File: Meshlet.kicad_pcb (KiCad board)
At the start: 2 copper layers, 60.2 x 39 mm, 98 parts, among them J1 Ext. Notif. Header, J10 STEMMA QT I2C, J11 GPIO Exp., J12 I2C PINHEADER, J2 USB_C_Receptacle_USB2.0_16P, J3 Ext. Power Header, J4 Batt. Header (JST-PH 2.0), J5 SWD, J6 Batt. Header (Picoblade 1.25), J7 GPS Header, J8 User Btn Header, J9 Power Switch, Q1 AO3400A, SW1 BOOTSEL, SW3 RST, U1 W25Q32JVZP, U2 XC6206PxxxMR, U3 RP2350_60QFN, U4 INA3221, U5 BME280, U6 Wio-SX1262, U7 USBLC6-2SC6, U8 BQ24074RGT, Y1 12.000MHz

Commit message: appease the trademark gods
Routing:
- net Net-(J9-Pin_1): track 14.3 -> 14.9 mm
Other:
- board text added: "HEY!"
- board text added: "PUT ME BACK!"

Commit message: docs
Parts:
- J7: footprint Connector_PinHeader_1.27mm:PinHeader_1x04_P1.27mm_Vertical -> Connector_PinHeader_1.27mm:PinHeader_1x05_P1.27mm_Vertical
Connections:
- U3 pad 8: unconnected-(U3-GPIO5-Pad8) -> GPS_EN
- U4 pad 5: GND -> I2C_SDA
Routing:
- net GPS_EN: track 0.00 -> 21.0 mm, vias 0 -> 1
- net I2C_SDA: track 107.4 -> 112.0 mm, vias 3 -> 4
- net Net-(U3-RUN): track 41.7 -> 44.7 mm
- net GND: track 23.7 -> 21.1 mm
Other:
- board text added: "3V"
- board text added: ":"
- board text added: "EN"
- board text added: "I HOPE YOU HAVE A LONG ENOUGH USB CABLE"
- board text added: "USR BTN"
- board text added: "https://5panel.dance/meshlet"
- board text added: "×1"

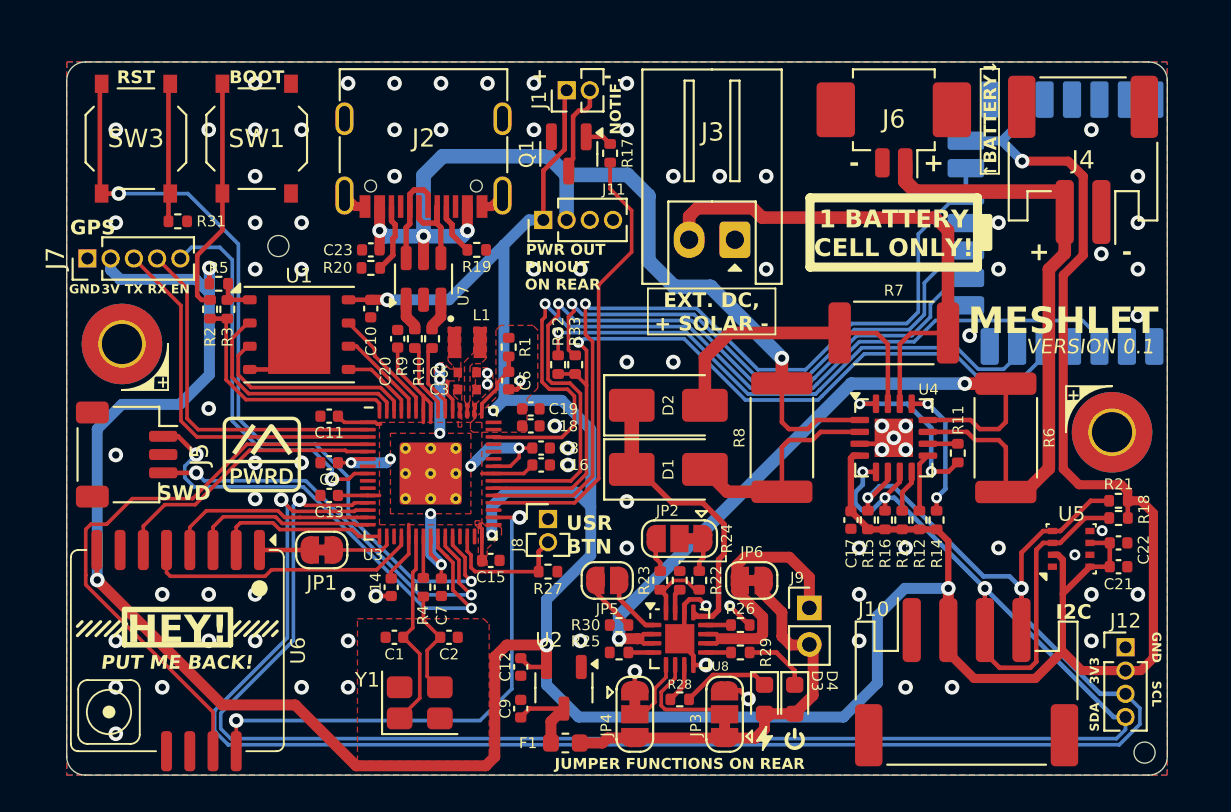
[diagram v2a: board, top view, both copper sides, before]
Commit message: Fixed stemma port pin order, more touchups
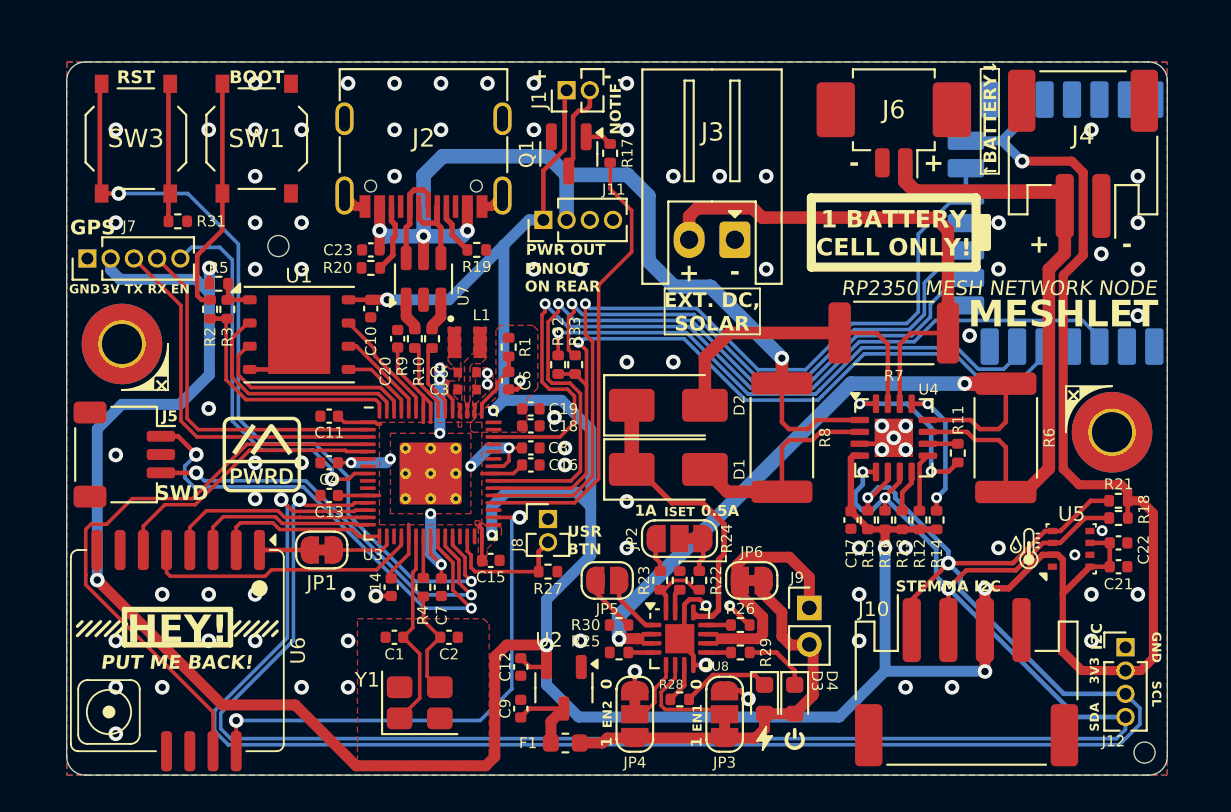
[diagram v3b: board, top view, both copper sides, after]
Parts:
- removed ?: , 
- added REF**: ToolingHole_1.152mm, MountingHole:ToolingHole_1.152mm, F.Cu at (121.8, 64.2)
- moved C16 0.57 mm to (135.6, 76.2)
- moved C8 0.56 mm to (135.6, 75.3)
- moved J4 0.33 mm to (165.8, 59.2)
- moved J5 0.13 mm to (113.4, 75.6)
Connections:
- J10 pad 1: GND -> I2C_SCL
- J10 pad 2: +3V3 -> I2C_SDA
- J10 pad 3: I2C_SDA -> +3V3
- J10 pad 4: I2C_SCL -> GND
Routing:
- net I2C_SCL: track 105.6 -> 110.2 mm
- net I2C_SDA: track 112.0 -> 109.1 mm
- net +3V3: track 256.3 -> 257.4 mm, vias 8 -> 10
- net +1V1: track 21.3 -> 20.3 mm
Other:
- board text added: "0"
- board text added: "0.5A"
- board text added: "1"
- board text added: "1A"
- board text added: "EN1"
- board text added: "EN2"
- board text added: "EXT. DC, SOLAR"
- board text added: "ISET"
- board text added: "RP2350 MESH NETWORK NODE"
- board text added: "STEMMA I2C"
- board text added: "V0.1"
- board text added: "https://5panel.dance/Meshlet"
- board text added: "×"
- board text removed: "EXT. DC, + SOLAR -"
- board text removed: "JUMPER FUNCTIONS ON REAR"
- board text removed: "https://5panel.dance/meshlet"

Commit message: Ground fill thermal spoke bug workaround for RM2
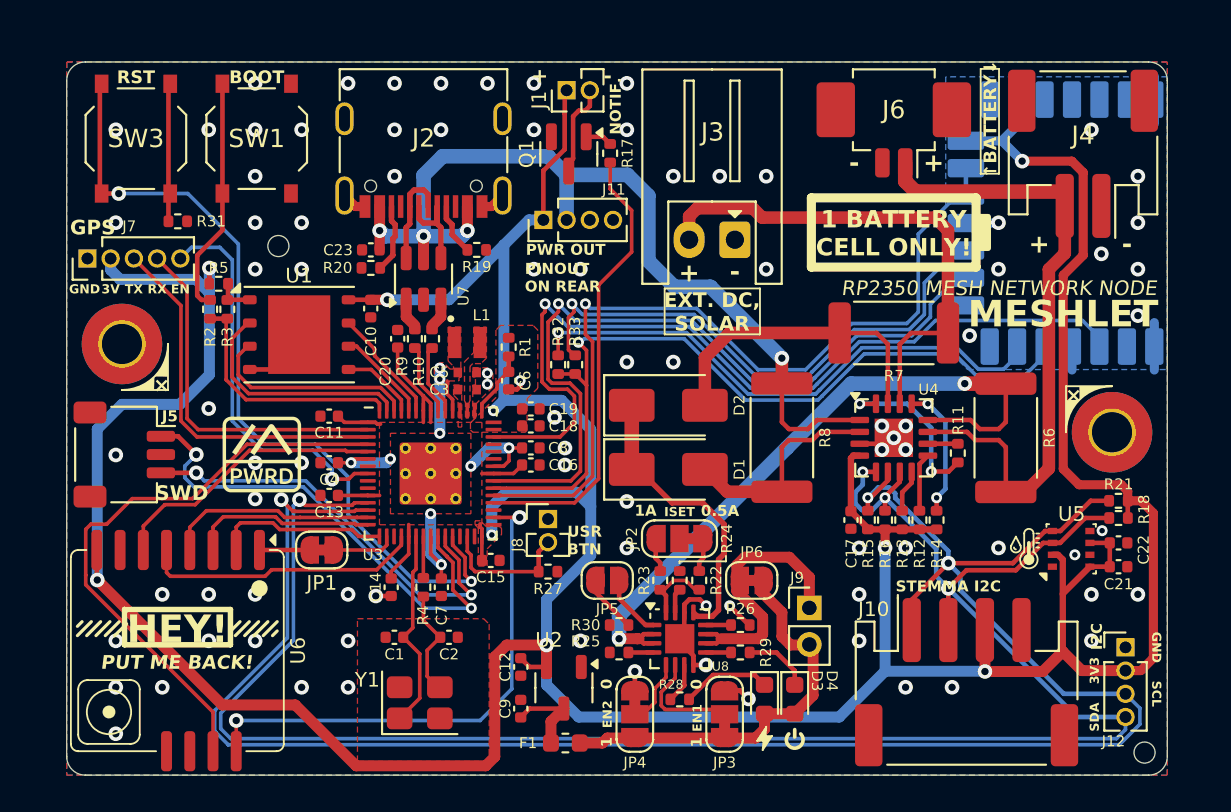
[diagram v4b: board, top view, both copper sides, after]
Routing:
- net GND: track 21.1 -> 29.6 mm
- net +3V3: track 257.4 -> 255.4 mm, vias 10 -> 9
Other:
- board text added: "GP0"
- board text added: "GP1"
- board text added: "GP22"
- board text added: "GP5"
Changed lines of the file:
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@@
 			(at -1.375 -1.375)
 			(size 0.6 0.6)
-			(drill 0.25)
+			(drill 0.3)
 			(layers "*.Cu")
 			(remove_unused_layers no)
@@
 			(at -1.375 0)
 			(size 0.6 0.6)
-			(drill 0.25)
+			(drill 0.3)
 			(layers "*.Cu")
 			(remove_unused_layers no)
@@
 			(at -1.375 1.375)
 			(size 0.6 0.6)
-			(drill 0.25)
+			(drill 0.3)
 			(layers "*.Cu")
 			(remove_unused_layers no)
@@
 			(at 0 -1.375)
 			(size 0.6 0.6)
-			(drill 0.25)
+			(drill 0.3)
 			(layers "*.Cu")
 			(remove_unused_layers no)
@@
 			(at 0 0)
 			(size 0.6 0.6)
-			(drill 0.25)
+			(drill 0.3)
 			(layers "*.Cu")
 			(remove_unused_layers no)
@@
 			(at 0 1.375)
 			(size 0.6 0.6)
-			(drill 0.25)
+			(drill 0.3)
 			(layers "*.Cu")
 			(remove_unused_layers no)
@@
 			(at 1.375 -1.375)
 			(size 0.6 0.6)
-			(drill 0.25)
+			(drill 0.3)
 			(layers "*.Cu")
 			(remove_unused_layers no)
@@
 			(at 1.375 0)
 			(size 0.6 0.6)
-			(drill 0.25)
+			(drill 0.3)
 			(layers "*.Cu")
 			(remove_unused_layers no)
@@
 			(at 1.375 1.375)
 			(size 0.6 0.6)
-			(drill 0.25)
+			(drill 0.3)
 			(layers "*.Cu")
 			(remove_unused_layers no)
@@
 			(pinfunction "1")
 			(pintype "passive")
+			(clearance 0.2)
 		)
 		(pad "2" smd roundrect
@@
 			(pinfunction "3")
 			(pintype "passive")
+			(clearance 0.2)
 		)
 		(pad "4" smd roundrect
@@
 			(net 1 "XIN")
 			(pintype "passive")
+			(clearance 0.2)
 		)
 		(embedded_fonts no)
@@
 			(net 3 "Net-(C2-Pad2)")
 			(pintype "passive")
+			(clearance 0.2)
 		)
 		(embedded_fonts no)
@@
 		)
 	)
+	(gr_text "GP22"
+		(at 139.827 56.7563 270)
+		(layer "B.SilkS")
+		(effects
+			(font
+				(size 0.5 0.5)
+				(thickness 0.125)
+				(bold yes)
+			)
+			(justify left bottom mirror)
+		)
+	)
 	(gr_text "RP2350 MESH NETWORK NODE RP2350 MESH NETWORK NODE RP2350 MESH"
 		(at 155.35 78.025 45)
@@
 		)
 	)
+	(gr_text "GP0"
+		(at 115.2144 65.6336 90)
+		(layer "B.SilkS")
+		(effects
+			(font
+				(size 0.5 0.5)
+				(thickness 0.125)
+				(bold yes)
+			)
+			(justify left mirror)
+		)
+	)
 	(gr_text "GND"
 		(at 138.86 60.53 90)
@@
 		)
 	)
+	(gr_text "GP1"
+		(at 113.9444 65.6336 90)
+		(layer "B.SilkS")
+		(effects
+			(font
+				(size 0.5 0.5)
+				(thickness 0.125)
+				(bold yes)
+			)
+			(justify left mirror)
+		)
+	)
+	(gr_text "GP5"
+		(at 116.4844 65.6336 90)
+		(layer "B.SilkS")
+		(effects
+			(font
+				(size 0.5 0.5)
+				(thickness 0.125)
+				(bold yes)
+			)
+			(justify left mirror)
+		)
+	)
 	(gr_text "×1"
 		(at 134.2771 65.8622 0)
@@
 	)
 	(segment
+		(start 159.4228 62.9856)
+		(end 161.185518 62.9856)
+		(width 0.5)
+		(layer "B.Cu")
+		(net 2)
+	)
+	(segment
+		(start 169.7228 56.2356)
+		(end 169.7228 56.0578)
+		(width 0.5)
+		(layer "B.Cu")
+		(net 2)
+	)
+	(segment
+		(start 169.7228 56.2356)
+		(end 169.7228 54.9656)
+		(width 0.5)
+		(layer "B.Cu")
+		(net 2)
+	)
+	(segment
+		(start 165.2228 69.7356)
+		(end 165.2228 71.0184)
+		(width 0.5)
+		(layer "B.Cu")
+		(net 2)
+	)
+	(segment
+		(start 169.7228 69.7356)
+		(end 169.7228 71.0184)
+		(width 0.5)
+		(layer "B.Cu")
+		(net 2)
+	)
+	(segment
+		(start 161.185518 62.9856)
+		(end 161.205518 62.9656)
+		(width 0.5)
+		(layer "B.Cu")
+		(net 2)
+	)
+	(segment
+		(start 169.7228 69.7356)
+		(end 169.7228 68.4276)
+		(width 0.5)
+		(layer "B.Cu")
+		(net 2)
+	)
+	(segment
+		(start 169.7228 56.2356)
+		(end 169.7228 57.5564)
+		(width 0.5)
+		(layer "B.Cu")
+		(net 2)
+	)
+	(segment
 		(start 129.76 83.404657)
 		(end 129.76 84.709508)
@@
 	)
 	(segment
-		(start 164.1512 81.1224)
-		(end 163.609554 81.1224)
-		(width 0.35)
-		(layer "F.Cu")
-		(net 4)
-	)
-	(segment
 		(start 132.86 79.594176)
 		(end 132.86 79.429308)
@@
 	)
 	(segment
+		(start 165.7604 87.4522)
+		(end 164.719 86.4108)
+		(width 0.6)
+		(layer "F.Cu")
+		(net 4)
+	)
+	(segment
 		(start 135.561899 87.2553)
 		(end 135.084399 86.7778)
@@
 	)
 	(segment
-		(start 164.719 86.4108)
-		(end 164.6936 86.4108)
-		(width 0.5)
-		(layer "F.Cu")
-		(net 4)
-	)
-	(segment
 		(start 126.7225 73.879308)
 		(end 127.145132 73.879308)
@@
 	)
 	(segment
+		(start 163.6268 87.503)
+		(end 164.719 86.4108)
+		(width 0.6)
+		(layer "F.Cu")
+		(net 4)
+	)
+	(segment
 		(start 162.4965 59.6011)
 		(end 165.2143 59.6011)
@@
 	)
 	(segment
+		(start 168.148 87.4522)
+		(end 165.7604 87.4522)
+		(width 0.6)
+		(layer "F.Cu")
+		(net 4)
+	)
+	(segment
 		(start 126.7225 77.879308)
 		(end 126.719592 77.8764)
@@
 	)
 	(segment
-		(start 161.775554 82.9564)
-		(end 160.4612 82.9564)
-		(width 0.35)
-		(layer "F.Cu")
-		(net 4)
-	)
-	(segment
 		(start 127.145132 73.879308)
 		(end 127.245132 73.979308)
@@
 	)
 	(segment
-		(start 163.609554 81.1224)
-		(end 161.775554 82.9564)
-		(width 0.35)
-		(layer "F.Cu")
-		(net 4)
-	)
-	(segment
 		(start 111.9124 80.8624)
 		(end 111.91 80.86)
@@
 	)
 	(segment
-		(start 160.4612 85.2372)
-		(end 160.4612 82.9564)
-		(width 0.6)
-		(layer "F.Cu")
-		(net 4)
-	)
-	(segment
-		(start 165.7604 87.4522)
-		(end 168.148 87.4522)
-		(width 0.5)
-		(layer "F.Cu")
-		(net 4)
-	)
-	(segment
 		(start 164.7444 65.8368)
 		(end 164.7444 76.4286)
@@
 	)
 	(segment
-		(start 164.719 86.4108)
-		(end 165.7604 87.4522)
-		(width 0.5)
-		(layer "F.Cu")
-		(net 4)
-	)
-	(segment
 		(start 130.16 73.241808)
 		(end 130.16 73.885308)
@@
 	)
 	(segment
+		(start 160.4645 87.503)
+		(end 163.6268 87.503)
+		(width 0.6)
+		(layer "F.Cu")
+		(net 4)
+	)
+	(segment
 		(start 164.4598 81.1224)
 		(end 164.719 81.3816)
@@
 	)
 	(via
-		(at 160.4612 82.9564)
-		(size 0.8)
-		(drill 0.4)
-		(layers "F.Cu" "B.Cu")
-		(net 4)
-	)
-	(via
 		(at 133.5024 80.0354)
 		(size 0.6)
@@
 	(segment
 		(start 153.1457 71.7643)
+		(end 149.64695 75.26305)
+		(width 0.8)
+		(layer "B.Cu")
+		(net 44)
+	)
+	(segment
+		(start 149.64695 75.26305)
 		(end 140.462 84.448)
 		(width 0.8)
@@
 		(priority 2)
 		(connect_pads
-			(clearance 0.2)
+			(clearance 0.1)
 		)
 		(min_thickness 0.2)
@@
 		(layers "F.Cu" "B.Cu")
 		(hatch edge 0.5)
-		(connect_pads thru_hole_only
+		(connect_pads
 			(clearance 0.1)
 		)
@@
 			)
 		)
+	)
+	(zone
+		(net 2)
+		(net_name "GND")
+		(layer "B.Cu")
+		(hatch edge 0.508)
+		(priority 9)
+		(connect_pads
+			(clearance 0.2)
+		)
+		(min_thickness 0.2)
+		(filled_areas_thickness no)
+		(fill yes
+			(thermal_gap 0.3)
+			(thermal_bridge_width 0.5)
+			(island_removal_mode 1)
+			(island_area_min 10)
+		)
+		(polygon
+			(pts
+				(xy 170.434 54.991) (xy 158.3182 54.991) (xy 158.3182 69.79285) (xy 159.51835 70.993) (xy 170.434 70.993)
+			)
+		)

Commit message: Better thermal relief bug workaround?
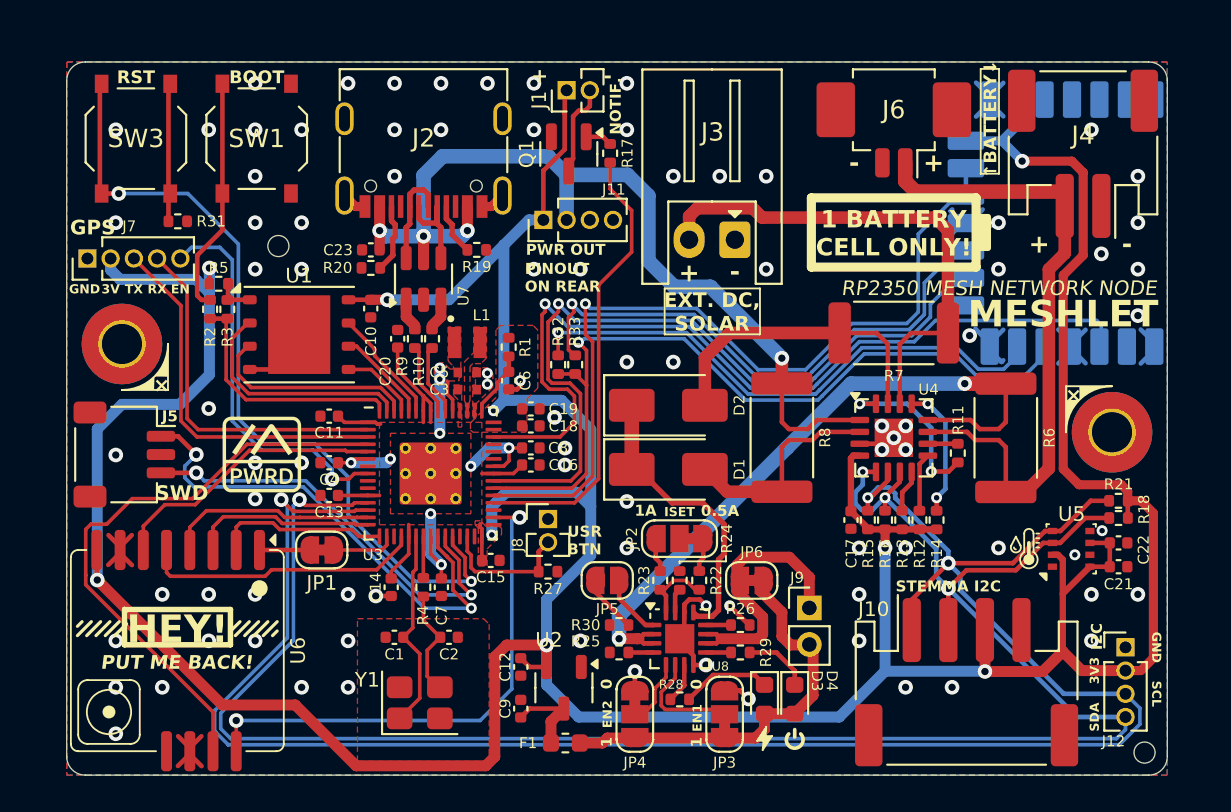
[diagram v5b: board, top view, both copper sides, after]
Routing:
- net GND: track 29.6 -> 50.1 mm

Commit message: Silkscreen changes, added BQ24074 output breakout
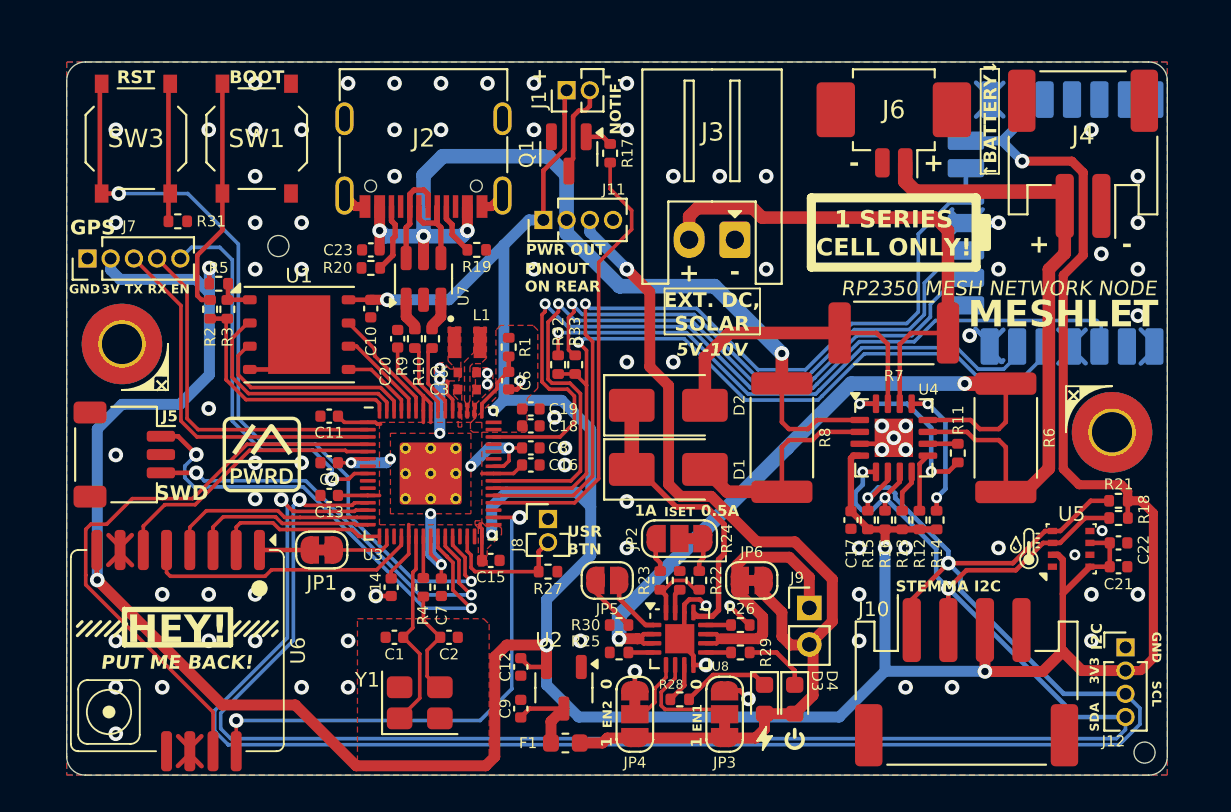
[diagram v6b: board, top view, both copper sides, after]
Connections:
- J11 pad 3: GND -> BMS_OUT
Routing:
- net BMS_OUT: track 22.4 -> 53.9 mm, vias 0 -> 1
- net INA_IN3-: track 50.5 -> 48.0 mm
- net GND: vias 89 -> 88
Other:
- board text added: "*4V4 MAX"
- board text added: "*BMS"
- board text added: "1 SERIES CELL ONLY!"
- board text added: "5V-10V"
- board text added: "LITHIUM ION & POLYMER"
- board text added: "MULTIPLE CELLS IN PARALLEL ARE OK IF YOU KNOW WHAT YOU'RE DOING"
- board text added: "OUTPUTS ONLY! **"
- board text added: "RP2350 MESH NETWORK NODE RP2350 MESH NETWORK NODE"
- board text added: "THE BQ24074 IS A 1-CELL SERIES CHARGER ONLY!"
- board text removed: "1 BATTERY CELL ONLY!"
- board text removed: "DO NOT ATTACH MORE THAN 1 CELL"
- board text removed: "RP2350 MESH NETWORK NODE RP2350 MESH NETWORK NODE RP2350 MESH"
- board text removed: "THE BQ24074 IS A SINGLE-CELL LIPO CHARGER ONLY!"
